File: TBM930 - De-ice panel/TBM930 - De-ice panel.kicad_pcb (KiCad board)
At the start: 2 copper layers, 190.5 x 101.6 mm, 83 parts, among them J1 SW_AIRFRAME_DE_ICE, J10 AVR-ISP-6, J11 Screw_Terminal_01x02, J2 SW_ICE_LIGHT, J3 SW_PROP_DE_ICE, J4 SW_WIND_SHIELD, J5 SW_PITOT_L_HTR, J6 SW_PITOT_R_HTR, J7 SW_INERT_SEP, J8 Barrel_Jack, J9 USB_B_Micro, U1 TLC5917IN, U2 TLC5917IN, U3 ATmega32U4-MU, Y1 Crystal_GND24

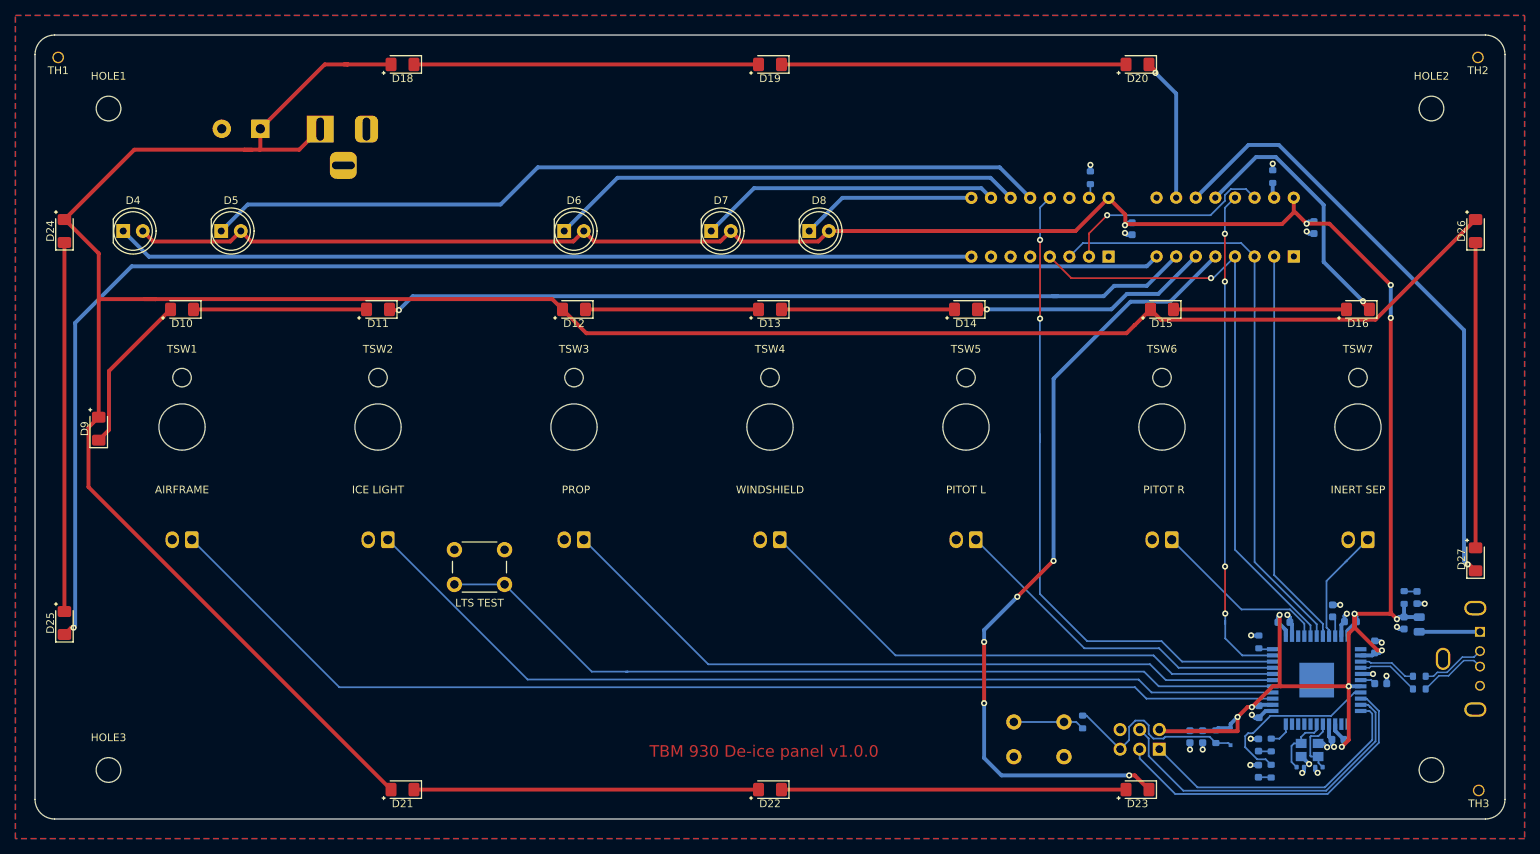
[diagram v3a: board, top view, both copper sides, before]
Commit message: Adjust the spacing of PCB components, reroute data trace
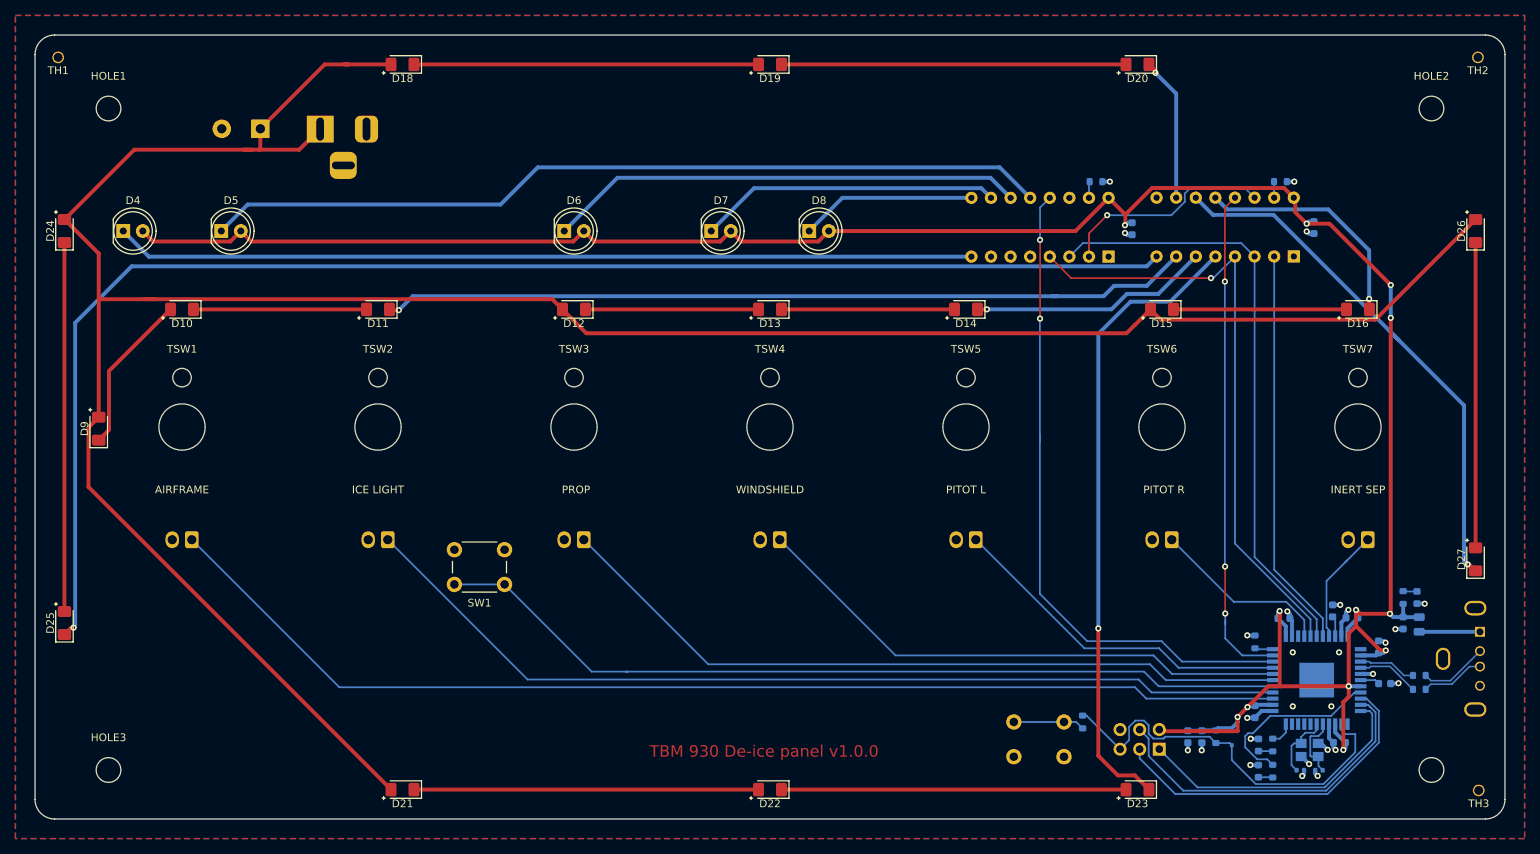
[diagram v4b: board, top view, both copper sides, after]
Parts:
- SW1: renamed from LTS TEST
- moved R4 1.19 mm to (200.8, 61.5), turned to 180 degrees
- moved R3 0.89 mm to (176.9, 61.5), turned to 180 degrees
- moved C4 0.54 mm to (210.0, 118.1)
- moved C5 0.52 mm to (197.5, 130.2)
- moved C1 0.50 mm to (213.5, 121.8)
- moved C2 0.50 mm to (201.2, 118.1)
- moved C7 0.50 mm to (214.3, 126.6)
- moved R11 0.50 mm to (197.5, 121.2)
- moved C3 0.45 mm to (208.4, 134.2)
- moved C16 0.40 mm to (203.3, 137.8)
- moved C17 0.40 mm to (205.8, 137.8)
- moved C12 0.27 mm to (188.8, 133.5)
- moved R2 0.20 mm to (199.8, 137.9)
- moved R5 0.19 mm to (199.8, 134.6)
- moved D17 0.16 mm to (194.5, 133.5)
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- renumbered RESET to SW2
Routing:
- net RESET: track 25.7 -> 51.9 mm
- net BACKLIGHT5: track 103.5 -> 82.4 mm, vias 5 -> 1
- net BACKLIGHT7: track 79.5 -> 69.9 mm
- net +5V: track 319.1 -> 323.7 mm
- net BACKLIGHT3: track 34.8 -> 30.4 mm
- net GND: track 32.6 -> 35.1 mm, vias 23 -> 27
- net /DR+: track 8.88 -> 8.26 mm
- net /DR-: track 8.39 -> 8.90 mm
- net Net-(R11-Pad1): track 1.85 -> 2.35 mm
- net Net-(C7-Pad1): track 2.01 -> 2.51 mm
- net BACKLIGHT_BRIGHT: vias 4 -> 3

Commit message: More footprint changes
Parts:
- C11: value 0.1uf -> 100nf; footprint Capacitor_SMD:C_0603_1608Metric -> Capacitor_SMD:C_0402_1005Metric
- C12, C2, C3, C4, C5, C8, C9: value 0.1uF -> 100nf; footprint Capacitor_SMD:C_0603_1608Metric -> Capacitor_SMD:C_0402_1005Metric
- C6, C7: footprint Capacitor_SMD:C_0603_1608Metric -> Capacitor_SMD:C_0402_1005Metric
- R10, R11, R2, R5, R6, R7, R8, R9: footprint Resistor_SMD:R_0603_1608Metric -> Resistor_SMD:R_0402_1005Metric
- R3, R4: footprint Resistor_SMD:R_0603_1608Metric -> Resistor_THT:R_Axial_DIN0207_L6.3mm_D2.5mm_P7.62mm_Horizontal
- moved R3 11.2 mm to (176.0, 50.3), turned to 270 degrees
- moved R4 11.2 mm to (200.0, 50.3), turned to 270 degrees
- moved C17 2.47 mm to (207.4, 135.9), turned to 90 degrees
- moved C16 2.45 mm to (201.8, 135.9), turned to 270 degrees
- moved C7 1.09 mm to (213.2, 126.9), turned to 270 degrees
- moved C3 0.88 mm to (207.8, 133.6)
- moved C9 0.17 mm to (181.4, 67.6)
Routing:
- net +5V: track 323.7 -> 316.5 mm, vias 12 -> 13
- net RESET: track 51.9 -> 56.5 mm
- net Net-(R4-Pad2): track 2.09 -> 5.66 mm
- net Net-(R3-Pad2): track 2.14 -> 5.69 mm
- net GND: track 35.1 -> 31.8 mm, vias 27 -> 23
- net /XTAL1: track 8.81 -> 6.15 mm

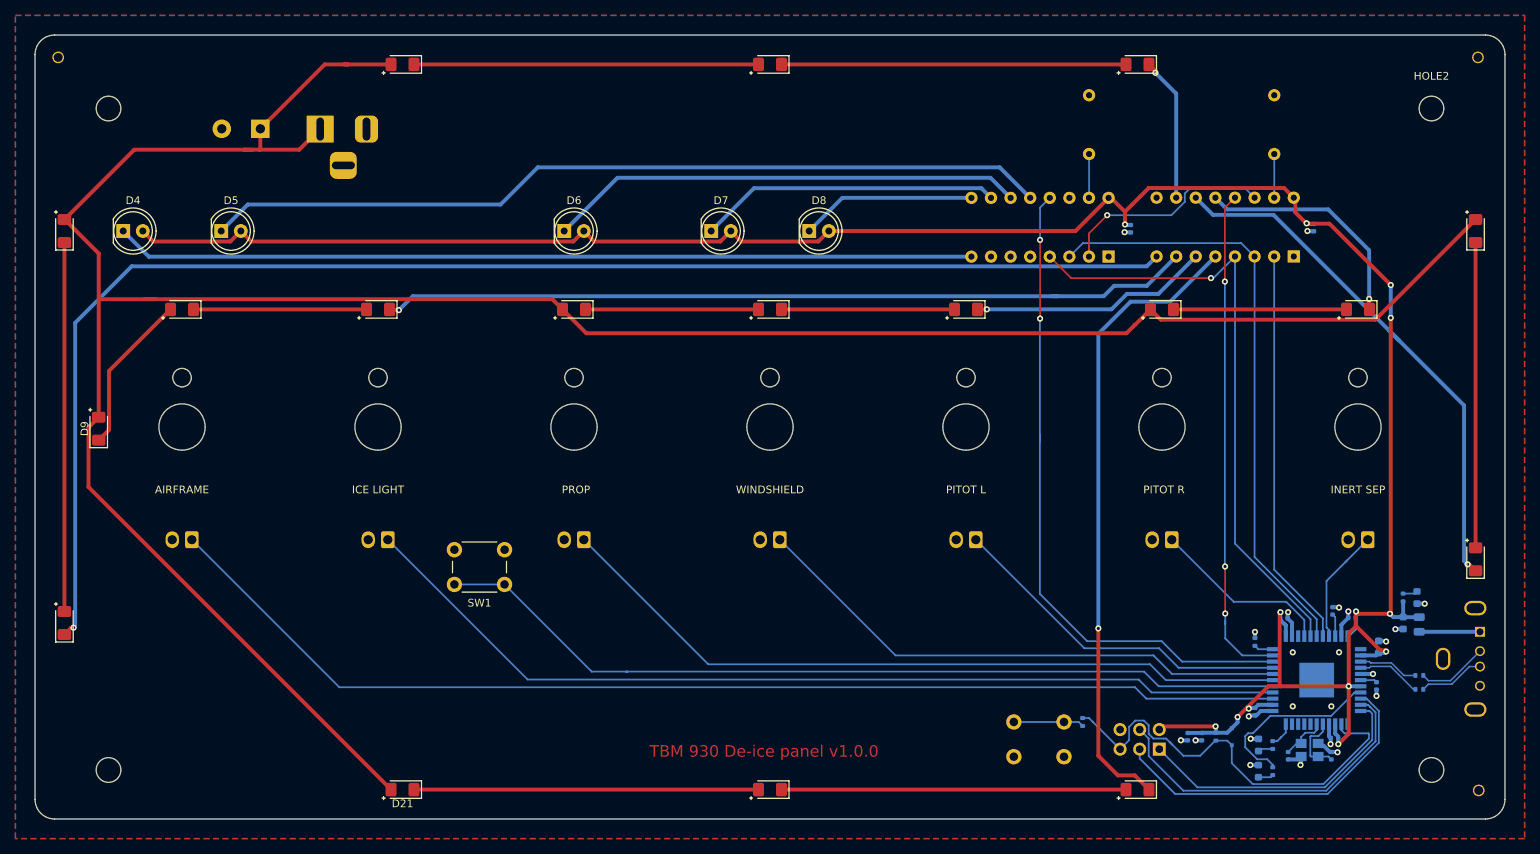
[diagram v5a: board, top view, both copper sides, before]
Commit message: Change connector, fix BOM
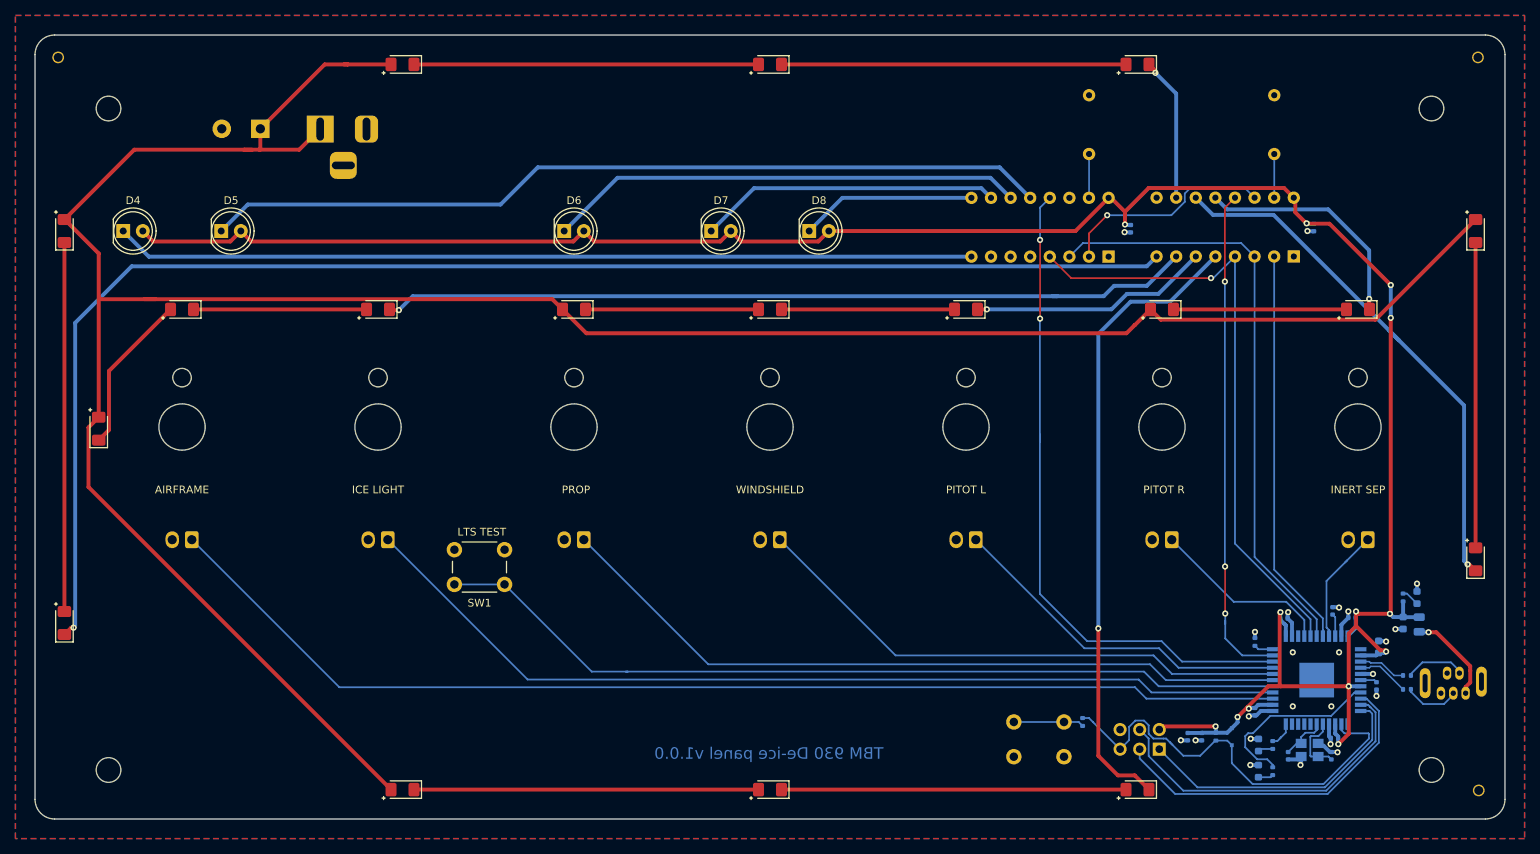
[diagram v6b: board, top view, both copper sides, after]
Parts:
- J9: value USB_B_Micro -> USB_B_Mini; footprint Global MobiFlight panel parts:USB_A_Molex_105057_Vertical -> Global MobiFlight panel parts:USB_B_Mini_Amphenol_UE25BE5510H
- moved J9 7.50 mm to (223.2, 126.5), turned to 0 degrees
- moved R7 1.60 mm to (217.2, 127.3)
- moved R8 1.60 mm to (217.2, 125.5)
- turned D3 to 270 degrees
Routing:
- net /VBUS: track 7.88 -> 12.2 mm, vias 0 -> 1
- net /D-: track 7.84 -> 6.24 mm
- net /D+: track 8.39 -> 6.79 mm
- net /DR+: track 8.58 -> 7.23 mm
- net /DR-: track 9.22 -> 7.92 mm
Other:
- board text added: "LTS TEST"
- board text added: "TBM 930 de-ice panel v1.0.0 Designed by: Neil Enns"
- board text removed: "SW_AIRFRAME_DE_ICE"
- board text removed: "SW_ICE_LIGHT"
- board text removed: "SW_INERT_SEP"
- board text removed: "SW_PITOT_L_HTR"
- board text removed: "SW_PITOT_R_HTR"
- board text removed: "SW_PROP_DE_ICE"
- board text removed: "SW_WIND_SHIELD"

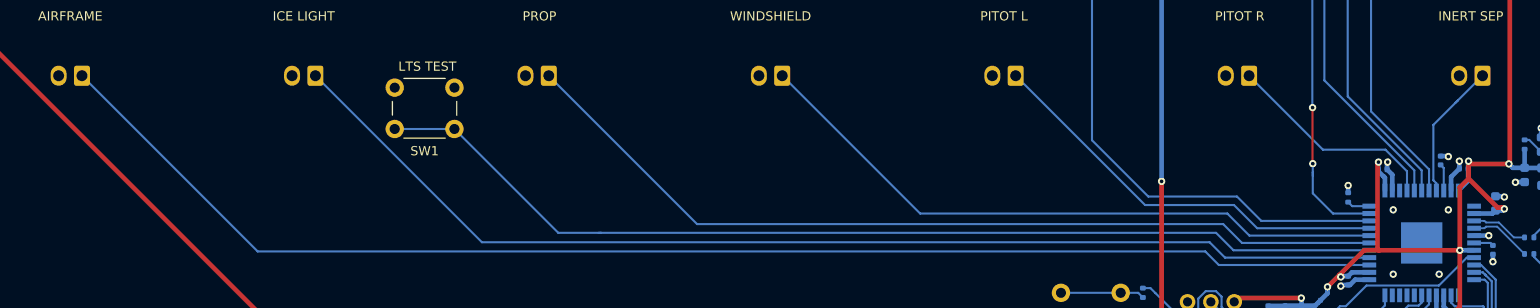
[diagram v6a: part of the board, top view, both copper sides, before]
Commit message: Breakout board and tbm930 board updates
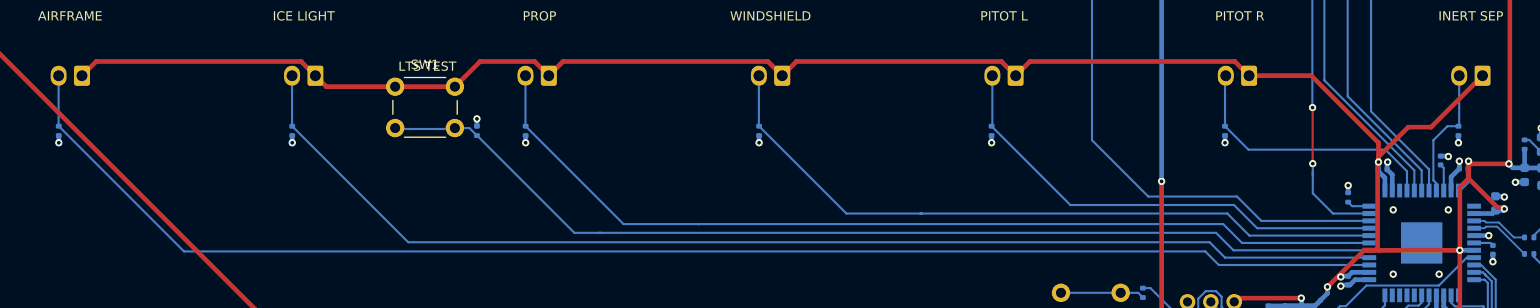
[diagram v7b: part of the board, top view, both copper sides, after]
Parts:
- added R1: 10k, Resistor_SMD:R_0402_1005Metric, B.Cu at (57.2, 114.0)
- added R12: 10k, Resistor_SMD:R_0402_1005Metric, B.Cu at (82.6, 114.0)
- added R13: 10k, Resistor_SMD:R_0402_1005Metric, B.Cu at (108.0, 114.0)
- added R14: 10k, Resistor_SMD:R_0402_1005Metric, B.Cu at (133.4, 114.0)
- added R15: 10k, Resistor_SMD:R_0402_1005Metric, B.Cu at (158.7, 114.0)
- added R16: 10k, Resistor_SMD:R_0402_1005Metric, B.Cu at (184.1, 114.0)
- added R17: 10k, Resistor_SMD:R_0402_1005Metric, B.Cu at (209.5, 114.0)
- added R18: 10k, Resistor_SMD:R_0402_1005Metric, B.Cu at (102.7, 114.0)
- C16, C17: value 20pF -> 20pf
- moved SW1 7.92 mm to (93.8, 109.1), turned to 0 degrees
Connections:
- J1 pad 1: SW_AIRFRAME -> +5V
- J1 pad 2: GND -> SW_AIRFRAME
- J2 pad 1: SW_ICE_LIGHT -> +5V
- J2 pad 2: GND -> SW_ICE_LIGHT
- J3 pad 1: SW_PROP -> +5V
- J3 pad 2: GND -> SW_PROP
- J4 pad 1: SW_WINDSHIELD -> +5V
- J4 pad 2: GND -> SW_WINDSHIELD
- J5 pad 1: SW_PITOT_L -> +5V
- J5 pad 2: GND -> SW_PITOT_L
- J6 pad 1: SW_PITOT_R -> +5V
- J6 pad 2: GND -> SW_PITOT_R
- J7 pad 1: SW_INERT_SEP -> +5V
- J7 pad 2: GND -> SW_INERT_SEP
- SW1 pad 1: SW_LTS_TEST -> +5V
- SW1 pad 2: GND -> SW_LTS_TEST
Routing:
- net +5V: track 316.5 -> 485.7 mm
- net GND: track 31.8 -> 38.0 mm, vias 23 -> 31
- net SW_PROP: track 96.8 -> 102.9 mm
- net SW_WINDSHIELD: track 71.1 -> 77.0 mm
- net SW_PITOT_L: track 45.4 -> 51.2 mm
- net SW_PITOT_R: track 23.6 -> 29.5 mm
- net SW_ICE_LIGHT: track 122.9 -> 128.6 mm
- net SW_AIRFRAME: track 148.6 -> 154.4 mm
- net SW_INERT_SEP: track 15.2 -> 14.5 mm
